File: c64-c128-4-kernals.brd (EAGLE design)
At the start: 21.3 x 40.6 mm, 15 parts, among them IC1 27C512, IC2 PIC12F629P

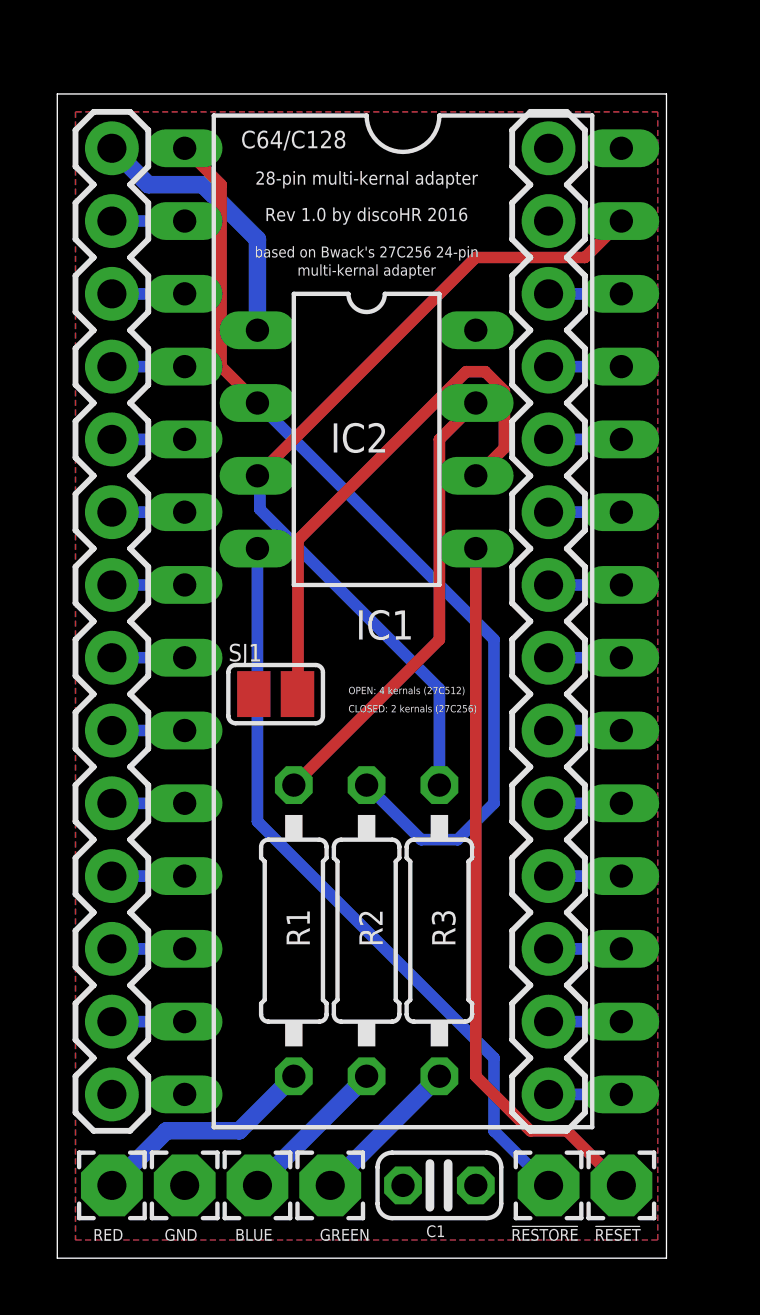
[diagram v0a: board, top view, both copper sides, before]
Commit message: added board images and PDF with schematic minor aesthetic changes on the silk layer
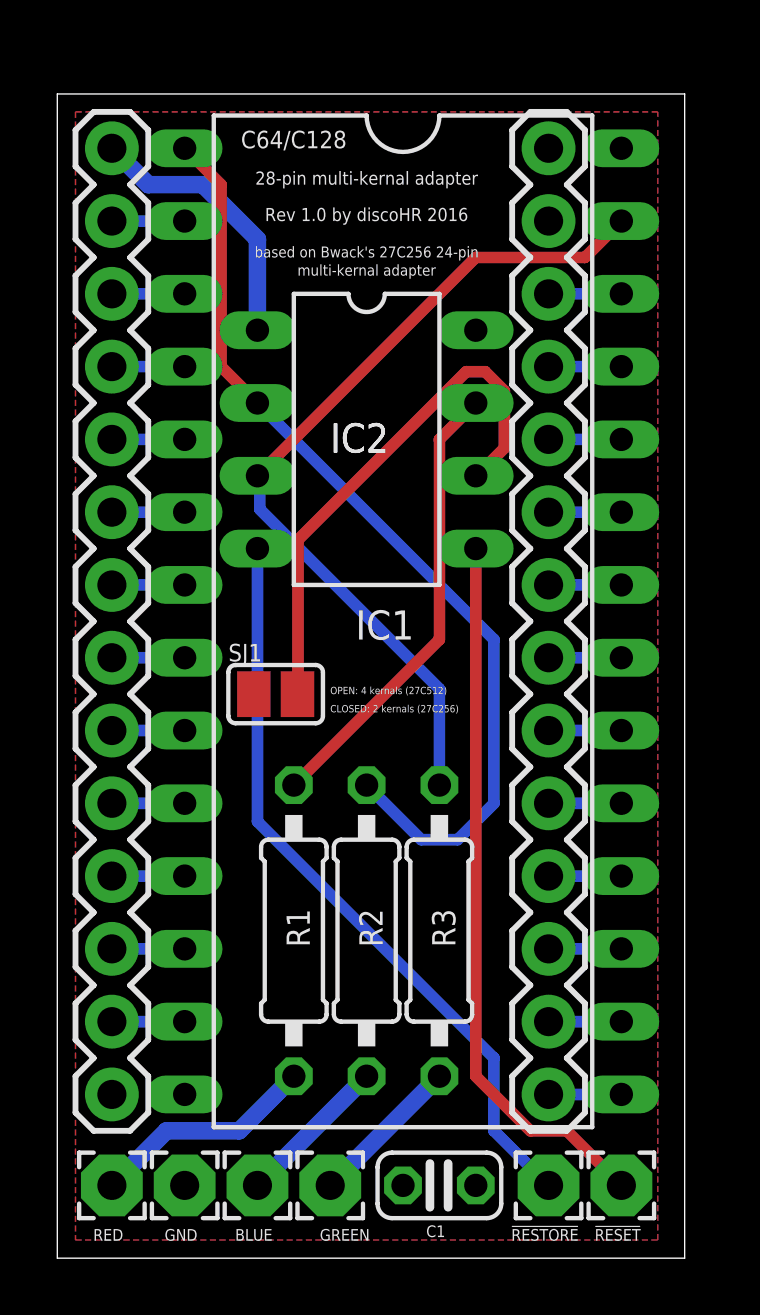
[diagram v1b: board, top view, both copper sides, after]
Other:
- board size 21.3 x 40.6 mm -> 21.9 x 40.6 mm
- board text added: "IC2"
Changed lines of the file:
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@@
 <layer number="123" name="tTestmark" color="7" fill="1" visible="yes" active="yes"/>
 <layer number="124" name="bTestmark" color="7" fill="1" visible="yes" active="yes"/>
-<layer number="125" name="_tNames" color="7" fill="1" visible="yes" active="yes"/>
+<layer number="125" name="_tNames" color="14" fill="1" visible="no" active="yes"/>
 <layer number="126" name="_bNames" color="7" fill="1" visible="yes" active="yes"/>
 <layer number="127" name="_tValues" color="7" fill="1" visible="yes" active="yes"/>
@@
 <board>
 <plain>
-<wire x1="0" y1="0" x2="21.26" y2="0" width="0" layer="20"/>
-<wire x1="21.26" y1="0" x2="21.26" y2="40.63" width="0" layer="20"/>
-<wire x1="21.26" y1="40.63" x2="0" y2="40.63" width="0" layer="20"/>
+<wire x1="0" y1="0" x2="21.895" y2="0" width="0" layer="20"/>
+<wire x1="21.895" y1="0" x2="21.895" y2="40.63" width="0" layer="20"/>
+<wire x1="21.895" y1="40.63" x2="0" y2="40.63" width="0" layer="20"/>
 <wire x1="0" y1="40.63" x2="0" y2="0" width="0" layer="20"/>
 <text x="10.795" y="36.195" size="0.4572" layer="25" font="vector" align="bottom-center">Rev 1.0 by discoHR 2016</text>
@@
 <text x="10.795" y="34.29" size="0.381" layer="25" font="vector" align="bottom-center">multi-kernal adapter</text>
 <text x="8.255" y="38.735" size="0.6096" layer="25" font="vector" align="bottom-center">C64/C128</text>
-<text x="10.16" y="19.685" size="0.254" layer="25">OPEN: 4 kernals (27C512)</text>
-<text x="10.16" y="19.05" size="0.254" layer="25">CLOSED: 2 kernals (27C256)</text>
+<text x="9.525" y="19.685" size="0.254" layer="25" font="vector">OPEN: 4 kernals (27C512)</text>
+<text x="9.525" y="19.05" size="0.254" layer="25" font="vector">CLOSED: 2 kernals (27C256)</text>
 <text x="15.24" y="36.195" size="0.6096" layer="26" rot="MR0" align="center-left">NC</text>
+<text x="9.525" y="28.1178" size="1.016" layer="25" ratio="10">IC2</text>
 </plain>
 <attributes>
@@
 </element>
 <element name="IC1" library="ic-package" package="DIL28-6" value="27C512" x="12.065" y="22.225" smashed="yes" rot="R270">
-<attribute name="NAME" x="11.43" y="21.59" size="1.016" layer="25" ratio="10" align="bottom-center"/>
+<attribute name="NAME" x="11.43" y="21.59" size="1.016" layer="25" font="vector" ratio="10" align="bottom-center"/>
 </element>
 <element name="IC2" library="microchip" package="DIL8" value="PIC12F629P" x="10.795" y="28.575" smashed="yes" rot="R270">
@@
 <attribute name="MF" value="MICROCHIP" x="10.795" y="28.575" size="1.778" layer="27" rot="R270" display="off"/>
 <attribute name="OC_NEWARK" value="67K0822" x="10.795" y="28.575" size="1.778" layer="27" rot="R270" display="off"/>
-<attribute name="NAME" x="9.525" y="28.1178" size="1.016" layer="25" ratio="10"/>
+<attribute name="NAME" x="9.525" y="28.1178" size="1.016" layer="25" font="vector" ratio="10"/>
 </element>
 <element name="J1" library="SparkFun-Connectors" package="1X14" value="" x="1.905" y="5.715" smashed="yes" rot="R90">
@@
 </element>
 <element name="R1" library="resistor" package="0207/10" value="2.2k" x="8.255" y="11.43" smashed="yes" rot="R90">
-<attribute name="NAME" x="8.001" y="12.192" size="0.8128" layer="25" ratio="10" rot="R90" align="top-right"/>
+<attribute name="NAME" x="8.001" y="12.192" size="0.8128" layer="25" font="vector" ratio="10" rot="R90" align="top-right"/>
 </element>
 <element name="R2" library="resistor" package="0207/10" value="2.2k" x="10.795" y="11.43" smashed="yes" rot="R90">
-<attribute name="NAME" x="10.541" y="12.192" size="0.8128" layer="25" ratio="10" rot="R90" align="top-right"/>
+<attribute name="NAME" x="10.541" y="12.192" size="0.8128" layer="25" font="vector" ratio="10" rot="R90" align="top-right"/>
 </element>
 <element name="R3" library="resistor" package="0207/10" value="2.2k" x="13.335" y="11.43" smashed="yes" rot="R90">
-<attribute name="NAME" x="13.081" y="12.192" size="0.8128" layer="25" ratio="10" rot="R90" align="top-right"/>
+<attribute name="NAME" x="13.081" y="12.192" size="0.8128" layer="25" font="vector" ratio="10" rot="R90" align="top-right"/>
 </element>
 <element name="RED" library="wirepad" package="2,15/1,0" value="" x="1.905" y="2.54" smashed="yes">
@@
 </element>
 <element name="SJ1" library="jumper" package="SJ" value="" x="7.62" y="19.685" smashed="yes">
-<attribute name="NAME" x="5.969" y="20.828" size="0.6096" layer="25" ratio="10"/>
+<attribute name="NAME" x="5.969" y="20.828" size="0.6096" layer="25" font="vector" ratio="10"/>
 <attribute name="VALUE" x="8.0201" y="19.685" size="0.02" layer="27"/>
 </element>

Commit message: moved pin headers to the bottom where they belong
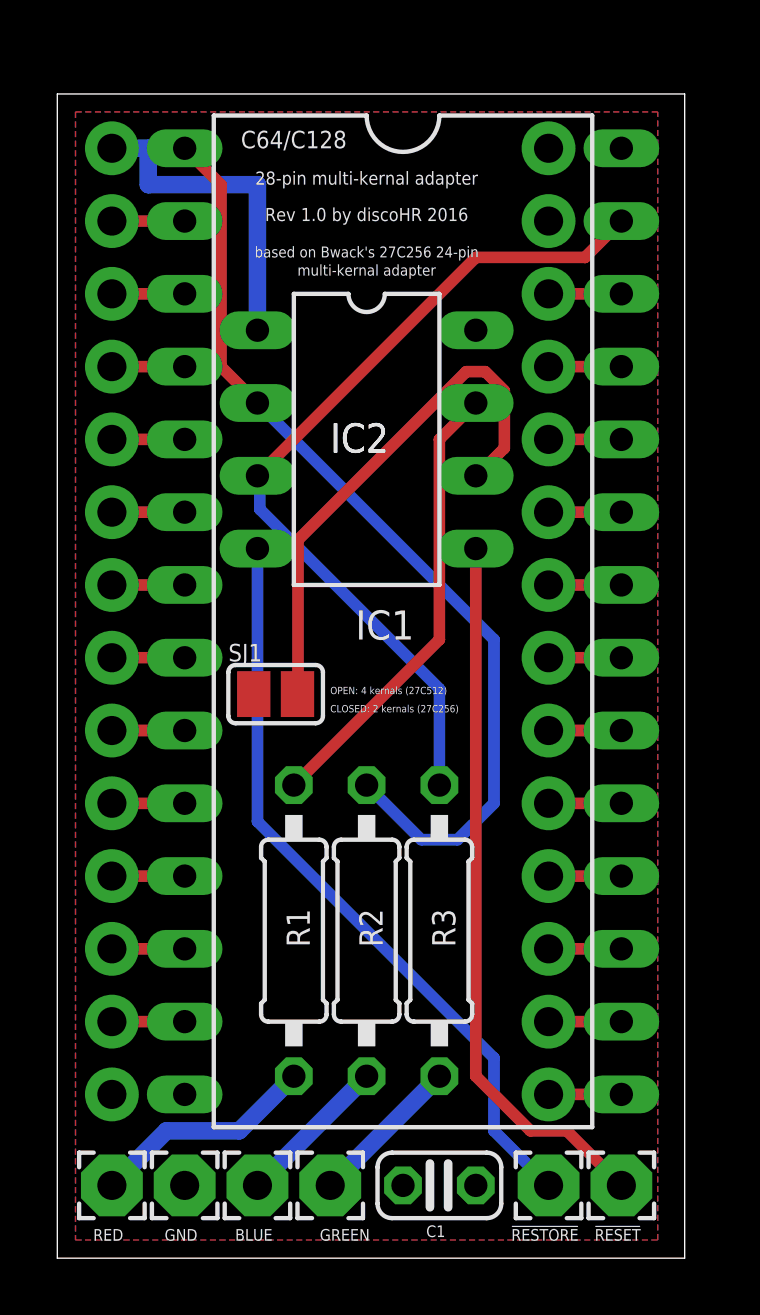
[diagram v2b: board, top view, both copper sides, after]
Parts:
- flipped J1 to the bottom
- flipped J2 to the bottom
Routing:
- net VCC: track 9.57 -> 11.4 mm
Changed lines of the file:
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@@
 <layer number="123" name="tTestmark" color="7" fill="1" visible="yes" active="yes"/>
 <layer number="124" name="bTestmark" color="7" fill="1" visible="yes" active="yes"/>
-<layer number="125" name="_tNames" color="14" fill="1" visible="no" active="yes"/>
+<layer number="125" name="_tNames" color="14" fill="1" visible="yes" active="yes"/>
 <layer number="126" name="_bNames" color="7" fill="1" visible="yes" active="yes"/>
 <layer number="127" name="_tValues" color="7" fill="1" visible="yes" active="yes"/>
@@
 <attribute name="NAME" x="9.525" y="28.1178" size="1.016" layer="25" font="vector" ratio="10"/>
 </element>
-<element name="J1" library="SparkFun-Connectors" package="1X14" value="" x="1.905" y="5.715" smashed="yes" rot="R90">
-<attribute name="VALUE" x="5.08" y="4.445" size="1.27" layer="27" rot="R90"/>
-</element>
-<element name="J2" library="SparkFun-Connectors" package="1X14" value="" x="17.145" y="5.715" smashed="yes" rot="R90">
-<attribute name="VALUE" x="20.32" y="4.445" size="1.27" layer="27" rot="R90"/>
+<element name="J1" library="SparkFun-Connectors" package="1X14" value="" x="1.905" y="5.715" smashed="yes" rot="MR90">
+<attribute name="VALUE" x="-1.27" y="4.445" size="1.27" layer="28" rot="MR90"/>
+</element>
+<element name="J2" library="SparkFun-Connectors" package="1X14" value="" x="17.145" y="5.715" smashed="yes" rot="MR90">
+<attribute name="VALUE" x="13.97" y="4.445" size="1.27" layer="28" rot="MR90"/>
 </element>
 <element name="R1" library="resistor" package="0207/10" value="2.2k" x="8.255" y="11.43" smashed="yes" rot="R90">
@@
 <vertex x="0.635" y="40.005"/>
 </polygon>
-<wire x1="6.985" y1="32.385" x2="6.985" y2="35.56" width="0.6096" layer="16"/>
-<wire x1="6.985" y1="35.56" x2="5.08" y2="37.465" width="0.6096" layer="16"/>
-<wire x1="5.08" y1="37.465" x2="3.175" y2="37.465" width="0.6096" layer="16"/>
-<wire x1="3.175" y1="37.465" x2="1.905" y2="38.735" width="0.6096" layer="16"/>
+<wire x1="1.905" y1="38.735" x2="3.175" y2="38.735" width="0.6096" layer="16"/>
+<wire x1="3.175" y1="38.735" x2="3.175" y2="37.465" width="0.6096" layer="16"/>
+<wire x1="3.175" y1="37.465" x2="6.985" y2="37.465" width="0.6096" layer="16"/>
+<wire x1="6.985" y1="37.465" x2="6.985" y2="32.385" width="0.6096" layer="16"/>
 </signal>
 <signal name="GND" class="1">
@@
 <contactref element="IC1" pad="15"/>
 <contactref element="J2" pad="1"/>
-<wire x1="17.145" y1="5.715" x2="19.685" y2="5.715" width="0.4064" layer="16"/>
+<wire x1="17.145" y1="5.715" x2="19.685" y2="5.715" width="0.4064" layer="1"/>
 </signal>
 <signal name="N$4">
 <contactref element="IC1" pad="16"/>
 <contactref element="J2" pad="2"/>
-<wire x1="17.145" y1="8.255" x2="19.685" y2="8.255" width="0.4064" layer="16"/>
+<wire x1="17.145" y1="8.255" x2="19.685" y2="8.255" width="0.4064" layer="1"/>
 </signal>
 <signal name="N$5">
 <contactref element="IC1" pad="17"/>
 <contactref element="J2" pad="3"/>
-<wire x1="17.145" y1="10.795" x2="19.685" y2="10.795" width="0.4064" layer="16"/>
+<wire x1="17.145" y1="10.795" x2="19.685" y2="10.795" width="0.4064" layer="1"/>
 </signal>
 <signal name="N$6">
 <contactref element="IC1" pad="18"/>
 <contactref element="J2" pad="4"/>
-<wire x1="19.685" y1="13.335" x2="17.145" y2="13.335" width="0.4064" layer="16"/>
+<wire x1="19.685" y1="13.335" x2="17.145" y2="13.335" width="0.4064" layer="1"/>
 </signal>
 <signal name="N$7">
 <contactref element="IC1" pad="19"/>
 <contactref element="J2" pad="5"/>
-<wire x1="19.685" y1="15.875" x2="17.145" y2="15.875" width="0.4064" layer="16"/>
+<wire x1="19.685" y1="15.875" x2="17.145" y2="15.875" width="0.4064" layer="1"/>
 </signal>
 <signal name="N$8">
 <contactref element="IC1" pad="20"/>
 <contactref element="J2" pad="6"/>
-<wire x1="19.685" y1="18.415" x2="17.145" y2="18.415" width="0.4064" layer="16"/>
+<wire x1="19.685" y1="18.415" x2="17.145" y2="18.415" width="0.4064" layer="1"/>
 </signal>
 <signal name="N$9">
 <contactref element="IC1" pad="21"/>
 <contactref element="J2" pad="7"/>
-<wire x1="19.685" y1="20.955" x2="17.145" y2="20.955" width="0.4064" layer="16"/>
+<wire x1="19.685" y1="20.955" x2="17.145" y2="20.955" width="0.4064" layer="1"/>
 </signal>
 <signal name="N$10">
 <contactref element="IC1" pad="22"/>
 <contactref element="J2" pad="8"/>
-<wire x1="19.685" y1="23.495" x2="17.145" y2="23.495" width="0.4064" layer="16"/>
+<wire x1="19.685" y1="23.495" x2="17.145" y2="23.495" width="0.4064" layer="1"/>
 </signal>
 <signal name="N$11">
 <contactref element="IC1" pad="23"/>
 <contactref element="J2" pad="9"/>
-<wire x1="19.685" y1="26.035" x2="17.145" y2="26.035" width="0.4064" layer="16"/>
+<wire x1="19.685" y1="26.035" x2="17.145" y2="26.035" width="0.4064" layer="1"/>
 </signal>
 <signal name="N$12">
 <contactref element="IC1" pad="24"/>
 <contactref element="J2" pad="10"/>
-<wire x1="19.685" y1="28.575" x2="17.145" y2="28.575" width="0.4064" layer="16"/>
+<wire x1="19.685" y1="28.575" x2="17.145" y2="28.575" width="0.4064" layer="1"/>
 </signal>
 <signal name="N$13">
 <contactref element="IC1" pad="25"/>
 <contactref element="J2" pad="11"/>
-<wire x1="19.685" y1="31.115" x2="17.145" y2="31.115" width="0.4064" layer="16"/>
+<wire x1="19.685" y1="31.115" x2="17.145" y2="31.115" width="0.4064" layer="1"/>
 </signal>
 <signal name="N$14">
 <contactref element="IC1" pad="26"/>
 <contactref element="J2" pad="12"/>
-<wire x1="19.685" y1="33.655" x2="17.145" y2="33.655" width="0.4064" layer="16"/>
+<wire x1="19.685" y1="33.655" x2="17.145" y2="33.655" width="0.4064" layer="1"/>
 </signal>
 <signal name="N$15">
 <contactref element="IC1" pad="2"/>
 <contactref element="J1" pad="13"/>
-<wire x1="1.905" y1="36.195" x2="4.445" y2="36.195" width="0.4064" layer="16"/>
+<wire x1="1.905" y1="36.195" x2="4.445" y2="36.195" width="0.4064" layer="1"/>
 </signal>
 <signal name="N$17">
 <contactref element="J1" pad="12"/>
 <contactref element="IC1" pad="3"/>
-<wire x1="1.905" y1="33.655" x2="4.445" y2="33.655" width="0.4064" layer="16"/>
+<wire x1="1.905" y1="33.655" x2="4.445" y2="33.655" width="0.4064" layer="1"/>
 </signal>
 <signal name="N$18">
 <contactref element="IC1" pad="4"/>
 <contactref element="J1" pad="11"/>
-<wire x1="1.905" y1="31.115" x2="4.445" y2="31.115" width="0.4064" layer="16"/>
+<wire x1="1.905" y1="31.115" x2="4.445" y2="31.115" width="0.4064" layer="1"/>
 </signal>
 <signal name="N$19">
 <contactref element="J1" pad="10"/>
 <contactref element="IC1" pad="5"/>
-<wire x1="1.905" y1="28.575" x2="4.445" y2="28.575" width="0.4064" layer="16"/>
+<wire x1="1.905" y1="28.575" x2="4.445" y2="28.575" width="0.4064" layer="1"/>
 </signal>
 <signal name="N$20">
 <contactref element="IC1" pad="6"/>
 <contactref element="J1" pad="9"/>
-<wire x1="1.905" y1="26.035" x2="4.445" y2="26.035" width="0.4064" layer="16"/>
+<wire x1="1.905" y1="26.035" x2="4.445" y2="26.035" width="0.4064" layer="1"/>
 </signal>
 <signal name="N$21">
 <contactref element="J1" pad="8"/>
 <contactref element="IC1" pad="7"/>
-<wire x1="1.905" y1="23.495" x2="4.445" y2="23.495" width="0.4064" layer="16"/>
+<wire x1="1.905" y1="23.495" x2="4.445" y2="23.495" width="0.4064" layer="1"/>
 </signal>
 <signal name="N$22">
 <contactref element="IC1" pad="8"/>
 <contactref element="J1" pad="7"/>
-<wire x1="1.905" y1="20.955" x2="4.445" y2="20.955" width="0.4064" layer="16"/>
+<wire x1="1.905" y1="20.955" x2="4.445" y2="20.955" width="0.4064" layer="1"/>
 </signal>
 <signal name="N$23">
 <contactref element="J1" pad="6"/>
 <contactref element="IC1" pad="9"/>
-<wire x1="1.905" y1="18.415" x2="4.445" y2="18.415" width="0.4064" layer="16"/>
+<wire x1="1.905" y1="18.415" x2="4.445" y2="18.415" width="0.4064" layer="1"/>
 </signal>
 <signal name="N$24">
 <contactref element="IC1" pad="10"/>
 <contactref element="J1" pad="5"/>
-<wire x1="1.905" y1="15.875" x2="4.445" y2="15.875" width="0.4064" layer="16"/>
+<wire x1="1.905" y1="15.875" x2="4.445" y2="15.875" width="0.4064" layer="1"/>
 </signal>
 <signal name="N$25">
 <contactref element="J1" pad="4"/>
 <contactref element="IC1" pad="11"/>
-<wire x1="1.905" y1="13.335" x2="4.445" y2="13.335" width="0.4064" layer="16"/>
+<wire x1="1.905" y1="13.335" x2="4.445" y2="13.335" width="0.4064" layer="1"/>
 </signal>
 <signal name="N$26">
 <contactref element="J1" pad="3"/>
 <contactref element="IC1" pad="12"/>
-<wire x1="1.905" y1="10.795" x2="4.445" y2="10.795" width="0.4064" layer="16"/>
+<wire x1="1.905" y1="10.795" x2="4.445" y2="10.795" width="0.4064" layer="1"/>
 </signal>
 <signal name="N$27">
 <contactref element="J1" pad="2"/>
 <contactref element="IC1" pad="13"/>
-<wire x1="1.905" y1="8.255" x2="4.445" y2="8.255" width="0.4064" layer="16"/>
+<wire x1="1.905" y1="8.255" x2="4.445" y2="8.255" width="0.4064" layer="1"/>
 </signal>
 <signal name="N$1">
